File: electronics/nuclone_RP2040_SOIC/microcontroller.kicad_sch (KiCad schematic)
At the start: 25 parts, among them J5 Conn_02x06_Odd_Even, U3 rp2040, U4 MX25L3233FZBI, Y1 12MHz

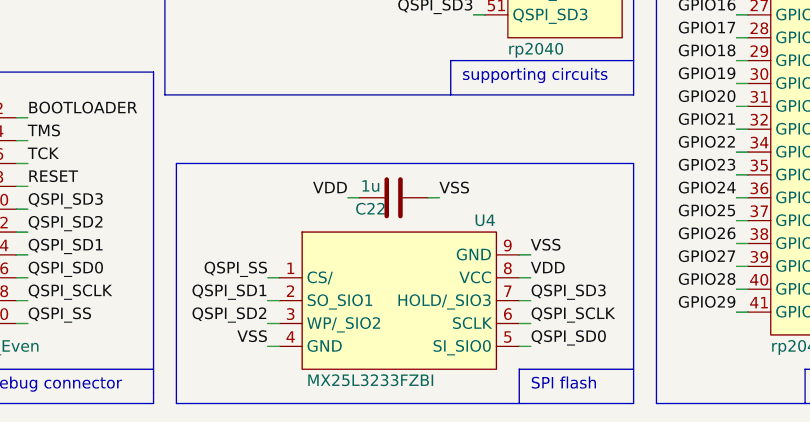
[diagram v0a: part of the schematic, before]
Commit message: placed and routed RP2040 nuclone with SOIC serial flash
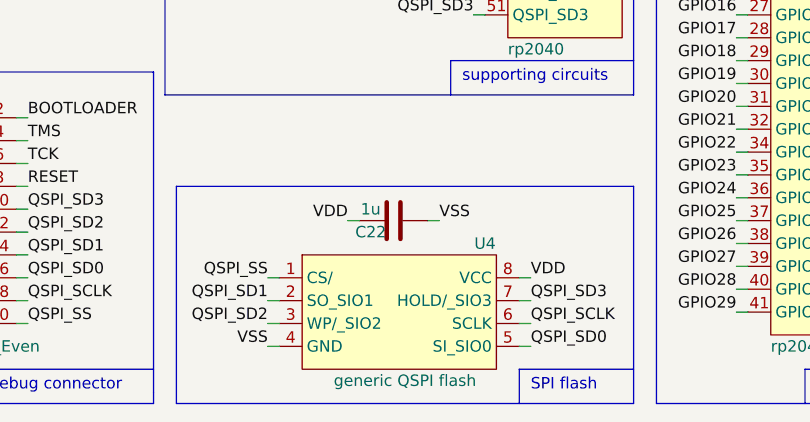
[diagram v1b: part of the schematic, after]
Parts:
- U4: value MX25L3233FZBI -> generic QSPI flash; footprint SquantorIC:USON-8-4x3-Macronix -> SquantorIC:SOIC-8_dual_wide; symbol SquantorGenericDigital:25X_9pin_QSPI_flash -> SquantorGenericDigital:25X_8pin_QSPI_flash
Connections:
- net VSS: no longer U4.9 (GND)
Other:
- moved on the sheet: C22
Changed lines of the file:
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@@
     (stroke (width 0) (type default) (color 0 0 0 0))
   )
-  (wire (pts (xy 217.17 139.7) (xy 218.44 139.7))
+  (wire (pts (xy 217.17 142.24) (xy 218.44 142.24))
     (stroke (width 0) (type default) (color 0 0 0 0))
   )
@@
     (stroke (width 0) (type default) (color 0 0 0 0))
   )
-  (polyline (pts (xy 248.92 162.56) (xy 248.92 135.89))
+  (polyline (pts (xy 248.92 162.56) (xy 248.92 138.43))
     (stroke (width 0) (type default) (color 0 0 0 0))
   )
@@
     (stroke (width 0) (type default) (color 0 0 0 0))
   )
-  (polyline (pts (xy 248.92 135.89) (xy 198.12 135.89))
+  (polyline (pts (xy 248.92 138.43) (xy 198.12 138.43))
     (stroke (width 0) (type default) (color 0 0 0 0))
   )
@@
     (stroke (width 0) (type default) (color 0 0 0 0))
   )
-  (polyline (pts (xy 198.12 135.89) (xy 198.12 162.56))
+  (polyline (pts (xy 198.12 138.43) (xy 198.12 162.56))
     (stroke (width 0) (type default) (color 0 0 0 0))
   )
@@
     (stroke (width 0) (type default) (color 0 0 0 0))
   )
-  (wire (pts (xy 236.22 146.05) (xy 237.49 146.05))
-    (stroke (width 0) (type default) (color 0 0 0 0))
-  )
   (wire (pts (xy 247.65 48.26) (xy 246.38 48.26))
     (stroke (width 0) (type default) (color 0 0 0 0))
@@
     (stroke (width 0) (type default) (color 0 0 0 0))
   )
-  (wire (pts (xy 226.06 139.7) (xy 227.33 139.7))
+  (wire (pts (xy 226.06 142.24) (xy 227.33 142.24))
     (stroke (width 0) (type default) (color 0 0 0 0))
   )
@@
     (effects (font (size 1.27 1.27)) (justify left bottom))
   )
-  (label "VDD" (at 217.17 139.7 180)
+  (label "VDD" (at 217.17 142.24 180)
     (effects (font (size 1.27 1.27)) (justify right bottom))
   )
@@
     (effects (font (size 1.27 1.27)) (justify right bottom))
   )
-  (label "VSS" (at 237.49 146.05 0)
-    (effects (font (size 1.27 1.27)) (justify left bottom))
-  )
   (label "QSPI_SD0" (at 181.61 148.59 0)
     (effects (font (size 1.27 1.27)) (justify left bottom))
@@
     (effects (font (size 1.27 1.27)) (justify right bottom))
   )
-  (label "VSS" (at 227.33 139.7 0)
+  (label "VSS" (at 227.33 142.24 0)
     (effects (font (size 1.27 1.27)) (justify left bottom))
   )
@@
     (pin "9")
   )
-  (symbol (lib_id "Device:C") (at 222.25 139.7 270) (unit 1)
+  (symbol (lib_id "Device:C") (at 222.25 142.24 270) (unit 1)
     (in_bom yes) (on_board yes)
-    (property "Reference" "C22" (id 0) (at 219.71 140.97 90))
-    (property "Value" "1u" (id 1) (at 219.71 138.43 90))
-    (property "Footprint" "SquantorRcl:C_0402" (id 2) (at 218.44 140.6652 0)
+    (property "Reference" "C22" (id 0) (at 219.71 143.51 90))
+    (property "Value" "1u" (id 1) (at 219.71 140.97 90))
+    (property "Footprint" "SquantorRcl:C_0402" (id 2) (at 218.44 143.2052 0)
       (effects (font (size 1.27 1.27)) hide)
     )
-    (property "Datasheet" "~" (id 3) (at 222.25 139.7 0)
+    (property "Datasheet" "~" (id 3) (at 222.25 142.24 0)
       (effects (font (size 1.27 1.27)) hide)
     )
@@
     (pin "2")
   )
-  (symbol (lib_id "SquantorGenericDigital:25X_9pin_QSPI_flash") (at 223.52 152.4 0) (unit 1)
+  (symbol (lib_id "SquantorGenericDigital:25X_8pin_QSPI_flash") (at 223.52 152.4 0) (unit 1)
     (in_bom yes) (on_board yes)
-    (property "Reference" "U4" (id 0) (at 232.41 142.24 0))
-    (property "Value" "MX25L3233FZBI" (id 1) (at 219.71 160.02 0))
-    (property "Footprint" "SquantorIC:USON-8-4x3-Macronix" (id 2) (at 223.52 152.4 0)
+    (property "Reference" "U4" (id 0) (at 232.41 144.78 0))
+    (property "Value" "generic QSPI flash" (id 1) (at 223.52 160.02 0))
+    (property "Footprint" "SquantorIC:SOIC-8_dual_wide" (id 2) (at 223.52 152.4 0)
       (effects (font (size 1.27 1.27)) hide)
     )
@@
     (pin "7")
     (pin "8")
-    (pin "9")
   )
   (symbol (lib_id "Device:R") (at 227.33 93.98 90) (unit 1)

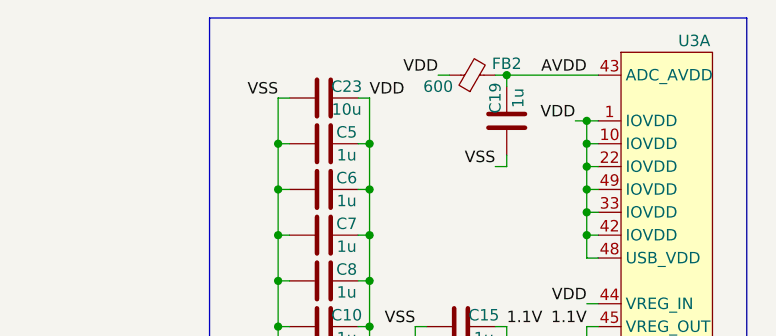
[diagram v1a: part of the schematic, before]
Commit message: fixed SOIC RP2040 nuclone errors
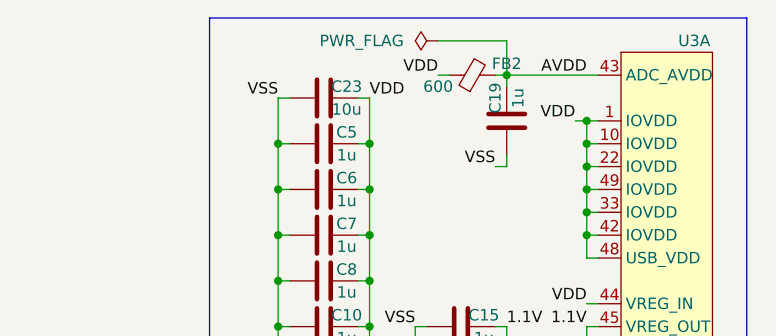
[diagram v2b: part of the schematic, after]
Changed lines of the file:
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@@
+    (stroke (width 0) (type default) (color 0 0 0 0))
+  )
+  (wire (pts (xy 256.54 16.51) (xy 256.54 20.32))
     (stroke (width 0) (type default) (color 0 0 0 0))
   )
@@
   )
   (wire (pts (xy 232.41 27.94) (xy 231.14 27.94))
+    (stroke (width 0) (type default) (color 0 0 0 0))
+  )
+  (wire (pts (xy 248.92 16.51) (xy 256.54 16.51))
     (stroke (width 0) (type default) (color 0 0 0 0))
   )
@@
     (pin "2")
   )
+  (symbol (lib_id "power:PWR_FLAG") (at 248.92 16.51 90) (unit 1)
+    (in_bom yes) (on_board yes) (fields_autoplaced)
+    (property "Reference" "#FLG0101" (id 0) (at 247.015 16.51 0)
+      (effects (font (size 1.27 1.27)) hide)
+    )
+    (property "Value" "PWR_FLAG" (id 1) (at 245.11 16.5099 90)
+      (effects (font (size 1.27 1.27)) (justify left))
+    )
+    (property "Footprint" "" (id 2) (at 248.92 16.51 0)
+      (effects (font (size 1.27 1.27)) hide)
+    )
+    (property "Datasheet" "~" (id 3) (at 248.92 16.51 0)
+      (effects (font (size 1.27 1.27)) hide)
+    )
+    (pin "1")
+  )
   (symbol (lib_id "Device:R") (at 226.06 99.06 90) (unit 1)
